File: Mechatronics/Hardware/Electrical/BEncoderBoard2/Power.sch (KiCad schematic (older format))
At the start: 23 parts, among them IC1 TP4056, IC2 DW01+G, J3 Barrel_Jack_Switch, J4 GNDPWR, J5 Conn_01x02_Male, Q1 DMosfet, Q2 Q_PMOS_GSD, U5 82402305, U6 LTC3240

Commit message: Changes
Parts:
- S1: value EG1218(+3.3v) -> EG1218_Conn
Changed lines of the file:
@@
 P 7900 3700
 F 0 "S1" H 7900 3375 50  0000 C CNN
-F 1 "EG1218(+3.3v)" H 8000 4000 50  0000 C CNN
+F 1 "EG1218_Conn" H 8000 4000 50  0000 C CNN
 F 2 "Encoder:PinHeader_1x04_P2.54mm_Vertical" H 8100 3900 50  0001 L CNN
 F 3 "http://spec_sheets.e-switch.com/specs/P040040.pdf" H 8100 4000 60  0001 L CNN

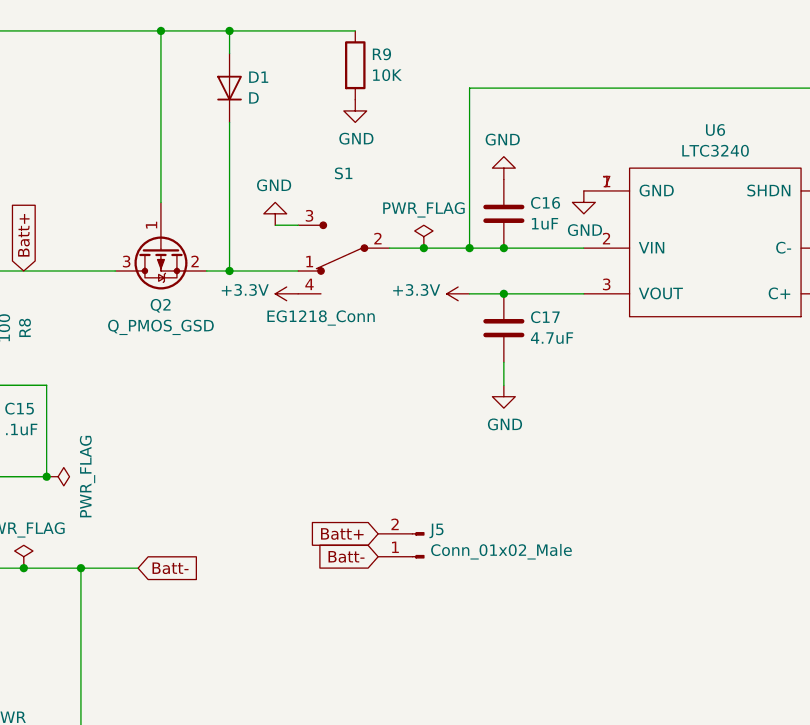
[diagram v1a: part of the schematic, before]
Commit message: pin header change
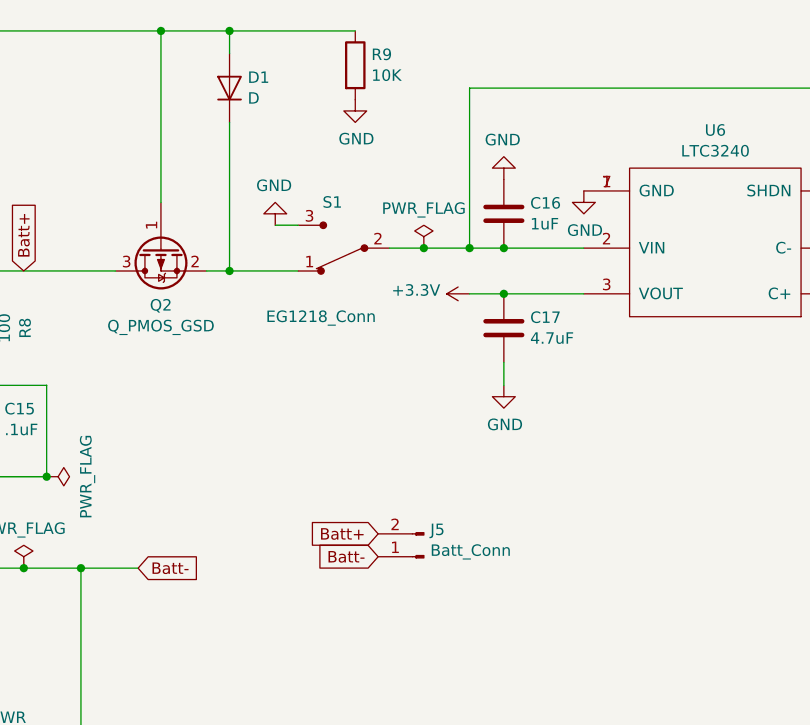
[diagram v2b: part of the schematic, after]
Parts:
- removed S1: EG1218_Conn, Encoder:PinHeader_1x04_P2.54mm_Vertical, symbol Encoder:EG1218(+3.3v)
- added S1: EG1218_Conn, Encoder:PinHeader_1x03_P2.54mm_Vertical, symbol Encoder:EG1218
- J5: value Conn_01x02_Male -> Batt_Conn
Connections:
- net GND: now also S1.3
- net at D1.1 (K), Q2.2 (S): now also S1.1
- net at C16.2, R10.1, U6.2 (VIN): now also S1.2
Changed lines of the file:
@@
 	1    0    0    -1
 $EndComp
-Wire Wire Line
-	7600 3600 7700 3600
 $Comp
 L power:GND #PWR?
@@
 	1    0    0    -1
 $EndComp
-Wire Wire Line
-	7700 3800 7400 3800
 Connection ~ 7400 3800
 $Comp
@@
 P 8250 5050
 F 0 "J5" H 8222 4932 50  0000 R CNN
-F 1 "Conn_01x02_Male" H 8222 5023 50  0000 R CNN
+F 1 "Batt_Conn" H 8222 5023 50  0000 R CNN
 F 2 "Encoder:PinHeader_1x02_P2.54mm_Vertical" H 8250 5050 50  0001 C CNN
 F 3 "~" H 8250 5050 50  0001 C CNN
@@
 Wire Wire Line
 	6500 5100 6750 5100
-$Comp
-L Encoder:EG1218(+3.3v) S1
-U 1 1 5F088668
+Wire Wire Line
+	7600 3600 7700 3600
+Wire Wire Line
+	7400 3800 7700 3800
+$Comp
+L Encoder:EG1218 S1
+U 1 1 5F1D7B37
 P 7900 3700
-F 0 "S1" H 7900 3375 50  0000 C CNN
+F 0 "S1" H 7950 3500 50  0000 C CNN
 F 1 "EG1218_Conn" H 8000 4000 50  0000 C CNN
-F 2 "Encoder:PinHeader_1x04_P2.54mm_Vertical" H 8100 3900 50  0001 L CNN
+F 2 "Encoder:PinHeader_1x03_P2.54mm_Vertical" H 8100 3900 50  0001 L CNN
 F 3 "http://spec_sheets.e-switch.com/specs/P040040.pdf" H 8100 4000 60  0001 L CNN
 F 4 "EG1903-ND" H 8100 4100 60  0001 L CNN "Digi-Key_PN"
@@
 	-1   0    0    1
 $EndComp
-$Comp
-L power:+3.3V #PWR?
-U 1 1 5F08D5F0
-P 7700 3900
-AR Path="/5F08D5F0" Ref="#PWR?"  Part="1"
-AR Path="/5F11DB77/5F08D5F0" Ref="#PWR0101"  Part="1"
-F 0 "#PWR0101" H 7700 3750 50  0001 C CNN
-F 1 "+3.3V" V 7715 4028 50  0000 L CNN
-F 2 "" H 7700 3900 50  0001 C CNN
-F 3 "" H 7700 3900 50  0001 C CNN
-	1    7700 3900
-	0    -1   -1   0
-$EndComp
 $EndSCHEMATC

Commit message: Changes
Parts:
- R6: value 1.2K -> 1.5K
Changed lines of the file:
@@
 AR Path="/5F11DB77/5F137077" Ref="R6"  Part="1"
 F 0 "R6" H 4100 4100 50  0000 L CNN
-F 1 "1.2K" H 4050 4000 50  0000 L CNN
+F 1 "1.5K" H 4050 4000 50  0000 L CNN
 F 2 "Encoder:R_0603_1608Metric_Pad1.05x0.95mm_HandSolder" V 4280 4050 50  0001 C CNN
 F 3 "~" H 4350 4050 50  0001 C CNN

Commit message: Changes
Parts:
- C15: value .1uF -> 100nF
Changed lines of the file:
@@
 AR Path="/5F11DB77/5F1370A8" Ref="C15"  Part="1"
 F 0 "C15" H 6415 4496 50  0000 L CNN
-F 1 ".1uF" H 6415 4405 50  0000 L CNN
+F 1 "100nF" H 6415 4405 50  0000 L CNN
 F 2 "Encoder:C_0603_1608Metric_Pad1.05x0.95mm_HandSolder" H 6338 4300 50  0001 C CNN
 F 3 "~" H 6300 4450 50  0001 C CNN

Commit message: PCB changes
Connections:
- net GND: now also IC1.9 (EP)
- no-connect marks 10 -> 9
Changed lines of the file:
@@
 Wire Wire Line
 	4550 3700 4600 3700
-NoConn ~ 5300 4300
 Wire Wire Line
 	6000 3500 6000 2750
@@
 	-1   0    0    1
 $EndComp
+$Comp
+L power:GND #PWR?
+U 1 1 5FF02BF1
+P 5300 4300
+F 0 "#PWR?" H 5300 4050 50  0001 C CNN
+F 1 "GND" H 5300 4150 50  0000 C CNN
+F 2 "" H 5300 4300 50  0001 C CNN
+F 3 "" H 5300 4300 50  0001 C CNN
+	1    5300 4300
+	1    0    0    -1
+$EndComp
 $EndSCHEMATC
